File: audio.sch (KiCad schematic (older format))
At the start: 51 parts, among them J1601 SJ-43515TS, SW1301 MIC_CAM_HKS, U1601 SGTL5000, U1602 PAM8301, U1603 FSA6157L6X

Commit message: Update the schematic symbols and footprints after upgrading to KiCad 5.0.0, fix all ERC and DRC violations after the new update/upgrade
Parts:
- C1601, C1602, C1603, C1604, C1605, C1606, C1607, C1608, C1611, C1612, C1613, C1614, C1615, C1616, C1617, C1618, C1619, C1620, C1621, C1622, C1623, C1624, C1625: footprint Capacitors_SMD:C_0603 -> Capacitor_SMD:C_0603_1608Metric; symbol dvk-mx8m-bsb-rescue:C -> Device:C
- C1609, C1610: footprint Capacitors_Tantalum_SMD:CP_Tantalum_Case-S_EIA-3216-12_Reflow -> Capacitor_Tantalum_SMD:CP_EIA-3216-12_Kemet-S; symbol dvk-mx8m-bsb-rescue:CP1 -> Device:CP1
- D1601, D1602: symbol dvk-mx8m-bsb-rescue:D_TVS_ALT -> Device:D_TVS_ALT
- D1603: symbol dvk-mx8m-bsb-rescue:D_Zener_ALT -> Device:D_Zener_ALT
- FB1601, FB1602, FB1603: symbol dvk-mx8m-bsb-rescue:Ferrite_Bead -> Device:Ferrite_Bead
- FB1604, FB1605, FB1606, FB1607, FB1608: symbol dvk-mx8m-bsb-rescue:Ferrite_Bead_Small -> Device:Ferrite_Bead_Small
- LS1601: symbol dvk-mx8m-bsb-rescue:Speaker -> Device:Speaker
- MK1601: symbol dvk-mx8m-bsb-rescue:Microphone -> Device:Microphone
- R1601, R1602, R1603, R1604, R1605, R1606, R1607, R1608: footprint Resistors_SMD:R_0603 -> Resistor_SMD:R_0603_1608Metric; symbol dvk-mx8m-bsb-rescue:R -> Device:R
- SW1301: symbol dvk-mx8m-bsb-rescue:SW_DPDT_x2 -> Switch:SW_DPDT_x2
- U1602: symbol dvk-mx8m-bsb-rescue:PAM8301 -> Amplifier_Audio:PAM8301
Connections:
- wire segments 134 -> 171

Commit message: Replace the CMC-6022-37T microphoen with the CMC-2242PBL-A THT one since the old one cannot be surface mounted/reflowed, add the microphone's 3D model
The microphone's pin position/order is agrees with the manufacturer's "measurement circuit" from the datasheet such that the right (facing the top of the mic) terminal/pin is its GND (-).
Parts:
- MK1601: value CMC-6022 -> CMC-2242PBL; Distrib Link https://www.digikey.com/product-detail/en/cui-inc/CMC-6022-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 -> https://www.digikey.com/product-detail/en/cui-inc/CMC-2242P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; Distrib PN 102-4095-ND -> 102-1727-ND; MFG Part Num CMC-6022-37T -> CMC-2242PBL-A; Others https://www.digikey.com/products/en/audio-products/microphones/158?k=&pkeyword=&pv966=678&pv966=281&pv966=434&pv966=469&pv966=428&pv966=292&pv966=522&pv966=525&pv966=481&pv966=551&pv966=1658&pv966=330&pv966=415&pv966=1367&pv966=317&pv966=395&FV=a40062%2C9340003%2C1f140000%2Cyr100Hz+~+20kHz%7C2145%2Cyr100Hz+~+80kHz%7C2145%2Cyr20Hz+~+20kHz%7C2145%2Cyr25Hz+~+20kHz%7C2145%2Cyr28Hz+~+20kHz%7C2145%2Cyr35Hz+~+20kHz%7C2145%2Cyr50Hz+~+20kHz%7C2145%2Cyr60Hz+~+20kHz%7C2145%2Cyr6Hz+~+20kHz%7C2145%2Cyr70Hz+~+20kHz%7C2145%2Cyr75Hz+~+20kHz%7C2145%2Cffe0009e&quantity=0&ColumnSort=1000011&page=1&pageSize=500 -> https://www.digikey.com/products/en/audio-products/microphones/158?FV=fffc0066%2Cffe0009e&quantity=0&ColumnSort=1000011&page=1&pageSize=25
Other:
- note removed: "Add TVS next to int-mic?\n(OpenMoko does this)"
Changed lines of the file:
@@
 P 9000 5350
 F 0 "MK1601" H 8850 5400 50  0000 R CNN
-F 1 "CMC-6022" H 8850 5325 50  0000 R CNN
+F 1 "CMC-2242PBL" H 8850 5325 50  0000 R CNN
 F 2 "dvk-mx8m-bsb:Electret_Condenser_Mic_6mm" V 9000 5450 50  0001 C CNN
-F 3 "https://www.cui.com/product/resource/cmc-6022-37t.pdf" V 9000 5450 50  0001 C CNN
+F 3 "https://www.cui.com/product/resource/cmc-2242pbl-a.pdf" V 9000 5450 50  0001 C CNN
 F 4 "CUI" H 9000 5350 60  0001 C CNN "MFG Name"
-F 5 "CMC-6022-37T" H 9000 5350 60  0001 C CNN "MFG Part Num"
-F 6 "102-4095-ND" H 9000 5350 60  0001 C CNN "Distrib PN"
-F 7 "https://www.digikey.com/product-detail/en/cui-inc/CMC-6022-37T/102-4095-ND/6561033" H 9000 5350 60  0001 C CNN "Distrib Link"
+F 5 "CMC-2242PBL-A" H 9000 5350 60  0001 C CNN "MFG Part Num"
+F 6 "102-1727-ND" H 9000 5350 60  0001 C CNN "Distrib PN"
+F 7 "https://www.digikey.com/product-detail/en/cui-inc/CMC-2242PBL-A/102-1727-ND/1869987" H 9000 5350 60  0001 C CNN "Distrib Link"
 F 8 "±3dB" H 9000 5350 60  0001 C CNN "Tolerance"
-F 9 "https://www.digikey.com/products/en/audio-products/microphones/158?k=&pkeyword=&pv966=678&pv966=281&pv966=434&pv966=469&pv966=428&pv966=292&pv966=522&pv966=525&pv966=481&pv966=551&pv966=1658&pv966=330&pv966=415&pv966=1367&pv966=317&pv966=395&FV=a40062%2C9340003%2C1f140000%2Cyr100Hz+~+20kHz%7C2145%2Cyr100Hz+~+80kHz%7C2145%2Cyr20Hz+~+20kHz%7C2145%2Cyr25Hz+~+20kHz%7C2145%2Cyr28Hz+~+20kHz%7C2145%2Cyr35Hz+~+20kHz%7C2145%2Cyr50Hz+~+20kHz%7C2145%2Cyr60Hz+~+20kHz%7C2145%2Cyr6Hz+~+20kHz%7C2145%2Cyr70Hz+~+20kHz%7C2145%2Cyr75Hz+~+20kHz%7C2145%2Cffe0009e&quantity=0&ColumnSort=1000011&page=1&pageSize=500" H 9000 5350 60  0001 C CNN "Others"
+F 9 "https://www.digikey.com/products/en/audio-products/microphones/158?FV=fffc0066%2Cffe0009e&quantity=0&ColumnSort=1000011&page=1&pageSize=25" H 9000 5350 60  0001 C CNN "Others"
 	1    9000 5350
 	-1   0    0    -1
@@
 	6250 2400 6250 2150
 Connection ~ 6250 2150
-Text Notes 9100 5650 0    60   ~ 0
-Add TVS next to int-mic?\n(OpenMoko does this)
 Text Notes 6510 2290 0    60   ~ 0
 8Ω

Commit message: Add new built-in mic's frequency response curve to the schematic and re-simulate the HP_DET pin circuit with the protection diode's SPICE model included
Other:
- note added: "Simulation of HP_DET\nwithout HP jack inserted:"
- note removed: "Simulation of HP_DET @ 1kHz output\n without HP jack inserted:"

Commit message: Reduce all 0603 resistor sizes to 0402
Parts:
- R1601, R1602, R1603, R1604, R1605, R1606, R1607, R1608: footprint Resistor_SMD:R_0603_1608Metric -> Resistor_SMD:R_0402_1005Metric
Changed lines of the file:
@@
 F 0 "R1603" H 5025 3850 50  0000 C CNN
 F 1 "33" H 4975 3750 50  0000 C CNN
-F 2 "Resistor_SMD:R_0603_1608Metric" V 4780 3800 50  0001 C CNN
+F 2 "Resistor_SMD:R_0402_1005Metric" V 4780 3800 50  0001 C CNN
 F 3 "" H 4850 3800 50  0001 C CNN
 	1    4850 3800
@@
 F 0 "R1604" H 5725 3700 50  0000 C CNN
 F 1 "15k" H 5675 3600 50  0000 C CNN
-F 2 "Resistor_SMD:R_0603_1608Metric" V 5480 3650 50  0001 C CNN
+F 2 "Resistor_SMD:R_0402_1005Metric" V 5480 3650 50  0001 C CNN
 F 3 "" H 5550 3650 50  0001 C CNN
 	1    5550 3650
@@
 F 0 "R1605" H 6075 3850 50  0000 C CNN
 F 1 "33" H 6025 3750 50  0000 C CNN
-F 2 "Resistor_SMD:R_0603_1608Metric" V 5830 3800 50  0001 C CNN
+F 2 "Resistor_SMD:R_0402_1005Metric" V 5830 3800 50  0001 C CNN
 F 3 "" H 5900 3800 50  0001 C CNN
 	1    5900 3800
@@
 F 0 "R1606" H 6775 3700 50  0000 C CNN
 F 1 "15k" H 6725 3600 50  0000 C CNN
-F 2 "Resistor_SMD:R_0603_1608Metric" V 6530 3650 50  0001 C CNN
+F 2 "Resistor_SMD:R_0402_1005Metric" V 6530 3650 50  0001 C CNN
 F 3 "" H 6600 3650 50  0001 C CNN
 	1    6600 3650
@@
 F 0 "R1607" V 6500 5450 50  0000 C CNN
 F 1 "2.2k" V 6700 5450 50  0000 C CNN
-F 2 "Resistor_SMD:R_0603_1608Metric" V 6530 5450 50  0001 C CNN
+F 2 "Resistor_SMD:R_0402_1005Metric" V 6530 5450 50  0001 C CNN
 F 3 "" H 6600 5450 50  0001 C CNN
 	1    6600 5450
@@
 F 0 "R1608" H 9825 2900 50  0000 C CNN
 F 1 "1M" H 9750 2800 50  0000 C CNN
-F 2 "Resistor_SMD:R_0603_1608Metric" V 9580 2850 50  0001 C CNN
+F 2 "Resistor_SMD:R_0402_1005Metric" V 9580 2850 50  0001 C CNN
 F 3 "" H 9650 2850 50  0001 C CNN
 	1    9650 2850
@@
 F 0 "R1601" H 3625 3700 50  0000 C CNN
 F 1 "NC" H 3550 3600 50  0000 C CNN
-F 2 "Resistor_SMD:R_0603_1608Metric" V 3380 3650 50  0001 C CNN
+F 2 "Resistor_SMD:R_0402_1005Metric" V 3380 3650 50  0001 C CNN
 F 3 "" H 3450 3650 50  0001 C CNN
 	1    3450 3650
@@
 F 0 "R1602" H 4475 2600 50  0000 C CNN
 F 1 "100k" H 4450 2500 50  0000 C CNN
-F 2 "Resistor_SMD:R_0603_1608Metric" V 4230 2550 50  0001 C CNN
+F 2 "Resistor_SMD:R_0402_1005Metric" V 4230 2550 50  0001 C CNN
 F 3 "" H 4300 2550 50  0001 C CNN
 	1    4300 2550

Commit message: Change all 0603 capacitors _EXCEPT_ the 2.2uF, 4.7uF, 8.2uF, 10uF, and 22uF caps to 0402
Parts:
- C1602, C1603, C1604, C1605, C1606, C1608, C1612, C1613, C1614, C1615, C1616, C1617, C1618, C1619, C1620, C1621, C1622, C1623, C1624, C1625: footprint Capacitor_SMD:C_0603_1608Metric -> Capacitor_SMD:C_0402_1005Metric
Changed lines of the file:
@@
 F 0 "C1606" H 3925 3550 50  0000 L CNN
 F 1 "NC" H 3925 3350 50  0000 L CNN
-F 2 "Capacitor_SMD:C_0603_1608Metric" H 3938 3300 50  0001 C CNN
+F 2 "Capacitor_SMD:C_0402_1005Metric" H 3938 3300 50  0001 C CNN
 F 3 "" H 3900 3450 50  0001 C CNN
 	1    3900 3450
@@
 F 0 "C1608" H 4225 3550 50  0000 L CNN
 F 1 "NC" H 4225 3350 50  0000 L CNN
-F 2 "Capacitor_SMD:C_0603_1608Metric" H 4238 3300 50  0001 C CNN
+F 2 "Capacitor_SMD:C_0402_1005Metric" H 4238 3300 50  0001 C CNN
 F 3 "" H 4200 3450 50  0001 C CNN
 	1    4200 3450
@@
 F 0 "C1624" H 8425 3550 50  0000 L CNN
 F 1 "270pF" H 8425 3350 50  0000 L CNN
-F 2 "Capacitor_SMD:C_0603_1608Metric" H 8438 3300 50  0001 C CNN
+F 2 "Capacitor_SMD:C_0402_1005Metric" H 8438 3300 50  0001 C CNN
 F 3 "" H 8400 3450 50  0001 C CNN
 	1    8400 3450
@@
 F 0 "C1621" H 6925 3550 50  0000 L CNN
 F 1 "270pF" H 6925 3350 50  0000 L CNN
-F 2 "Capacitor_SMD:C_0603_1608Metric" H 6938 3300 50  0001 C CNN
+F 2 "Capacitor_SMD:C_0402_1005Metric" H 6938 3300 50  0001 C CNN
 F 3 "" H 6900 3450 50  0001 C CNN
 	1    6900 3450
@@
 F 0 "C1612" H 4875 3550 50  0000 L CNN
 F 1 "100nF" H 4875 3350 50  0000 L CNN
-F 2 "Capacitor_SMD:C_0603_1608Metric" H 4888 3300 50  0001 C CNN
+F 2 "Capacitor_SMD:C_0402_1005Metric" H 4888 3300 50  0001 C CNN
 F 3 "" H 4850 3450 50  0001 C CNN
 	1    4850 3450
@@
 F 0 "C1614" H 5225 3750 50  0000 L CNN
 F 1 "100pF" H 5225 3550 50  0000 L CNN
-F 2 "Capacitor_SMD:C_0603_1608Metric" H 5238 3500 50  0001 C CNN
+F 2 "Capacitor_SMD:C_0402_1005Metric" H 5238 3500 50  0001 C CNN
 F 3 "" H 5200 3650 50  0001 C CNN
 	1    5200 3650
@@
 F 0 "C1615" H 5925 3550 50  0000 L CNN
 F 1 "100nF" H 5925 3350 50  0000 L CNN
-F 2 "Capacitor_SMD:C_0603_1608Metric" H 5938 3300 50  0001 C CNN
+F 2 "Capacitor_SMD:C_0402_1005Metric" H 5938 3300 50  0001 C CNN
 F 3 "" H 5900 3450 50  0001 C CNN
 	1    5900 3450
@@
 F 0 "C1618" H 6275 3750 50  0000 L CNN
 F 1 "100pF" H 6275 3550 50  0000 L CNN
-F 2 "Capacitor_SMD:C_0603_1608Metric" H 6288 3500 50  0001 C CNN
+F 2 "Capacitor_SMD:C_0402_1005Metric" H 6288 3500 50  0001 C CNN
 F 3 "" H 6250 3650 50  0001 C CNN
 	1    6250 3650
@@
 F 0 "C1605" H 3125 3750 50  0000 L CNN
 F 1 "100nF" H 3125 3550 50  0000 L CNN
-F 2 "Capacitor_SMD:C_0603_1608Metric" H 3138 3500 50  0001 C CNN
+F 2 "Capacitor_SMD:C_0402_1005Metric" H 3138 3500 50  0001 C CNN
 F 3 "" H 3100 3650 50  0001 C CNN
 	1    3100 3650
@@
 F 0 "C1622" H 7325 5500 50  0000 L CNN
 F 1 "270pF" H 7325 5300 50  0000 L CNN
-F 2 "Capacitor_SMD:C_0603_1608Metric" H 7338 5250 50  0001 C CNN
+F 2 "Capacitor_SMD:C_0402_1005Metric" H 7338 5250 50  0001 C CNN
 F 3 "" H 7300 5400 50  0001 C CNN
 	1    7300 5400
@@
 F 0 "C1620" V 6725 5100 50  0000 L CNN
 F 1 "100nF" V 6550 5250 50  0000 L CNN
-F 2 "Capacitor_SMD:C_0603_1608Metric" H 6638 5050 50  0001 C CNN
+F 2 "Capacitor_SMD:C_0402_1005Metric" H 6638 5050 50  0001 C CNN
 F 3 "" H 6600 5200 50  0001 C CNN
 	1    6600 5200
@@
 F 0 "C1619" H 6425 5750 50  0000 L CNN
 F 1 "1uF" H 6425 5550 50  0000 L CNN
-F 2 "Capacitor_SMD:C_0603_1608Metric" H 6438 5500 50  0001 C CNN
+F 2 "Capacitor_SMD:C_0402_1005Metric" H 6438 5500 50  0001 C CNN
 F 3 "" H 6400 5650 50  0001 C CNN
 	1    6400 5650
@@
 F 0 "C1602" H 1875 1700 50  0000 L CNN
 F 1 "100nF" H 1875 1500 50  0000 L CNN
-F 2 "Capacitor_SMD:C_0603_1608Metric" H 1888 1450 50  0001 C CNN
+F 2 "Capacitor_SMD:C_0402_1005Metric" H 1888 1450 50  0001 C CNN
 F 3 "" H 1850 1600 50  0001 C CNN
 	1    1850 1600
@@
 F 0 "C1603" H 2525 1500 50  0000 L CNN
 F 1 "100nF" H 2525 1300 50  0000 L CNN
-F 2 "Capacitor_SMD:C_0603_1608Metric" H 2538 1250 50  0001 C CNN
+F 2 "Capacitor_SMD:C_0402_1005Metric" H 2538 1250 50  0001 C CNN
 F 3 "" H 2500 1400 50  0001 C CNN
 	1    2500 1400
@@
 F 0 "C1604" H 3125 2115 50  0000 L CNN
 F 1 "100nF" H 3125 1900 50  0000 L CNN
-F 2 "Capacitor_SMD:C_0603_1608Metric" H 3138 1850 50  0001 C CNN
+F 2 "Capacitor_SMD:C_0402_1005Metric" H 3138 1850 50  0001 C CNN
 F 3 "" H 3100 2000 50  0001 C CNN
 	1    3100 2000
@@
 F 0 "C1625" H 8625 4450 50  0000 L CNN
 F 1 "10nF" H 8625 4250 50  0000 L CNN
-F 2 "Capacitor_SMD:C_0603_1608Metric" H 8638 4200 50  0001 C CNN
+F 2 "Capacitor_SMD:C_0402_1005Metric" H 8638 4200 50  0001 C CNN
 F 3 "" H 8600 4350 50  0001 C CNN
 	1    8600 4350
@@
 F 0 "C1623" H 8225 4450 50  0000 L CNN
 F 1 "100nF" H 8225 4250 50  0000 L CNN
-F 2 "Capacitor_SMD:C_0603_1608Metric" H 8238 4200 50  0001 C CNN
+F 2 "Capacitor_SMD:C_0402_1005Metric" H 8238 4200 50  0001 C CNN
 F 3 "" H 8200 4350 50  0001 C CNN
 	1    8200 4350
@@
 F 0 "C1616" H 6075 2650 50  0000 L CNN
 F 1 "220pF" H 6075 2450 50  0000 L CNN
-F 2 "Capacitor_SMD:C_0603_1608Metric" H 6088 2400 50  0001 C CNN
+F 2 "Capacitor_SMD:C_0402_1005Metric" H 6088 2400 50  0001 C CNN
 F 3 "" H 6050 2550 50  0001 C CNN
 	1    6050 2550
@@
 F 0 "C1617" H 6275 2650 50  0000 L CNN
 F 1 "220pF" H 6275 2450 50  0000 L CNN
-F 2 "Capacitor_SMD:C_0603_1608Metric" H 6288 2400 50  0001 C CNN
+F 2 "Capacitor_SMD:C_0402_1005Metric" H 6288 2400 50  0001 C CNN
 F 3 "" H 6250 2550 50  0001 C CNN
 	1    6250 2550
@@
 F 0 "C1613" H 4925 1550 50  0000 L CNN
 F 1 "1uF" H 4925 1350 50  0000 L CNN
-F 2 "Capacitor_SMD:C_0603_1608Metric" H 4938 1300 50  0001 C CNN
+F 2 "Capacitor_SMD:C_0402_1005Metric" H 4938 1300 50  0001 C CNN
 F 3 "" H 4900 1450 50  0001 C CNN
 	1    4900 1450

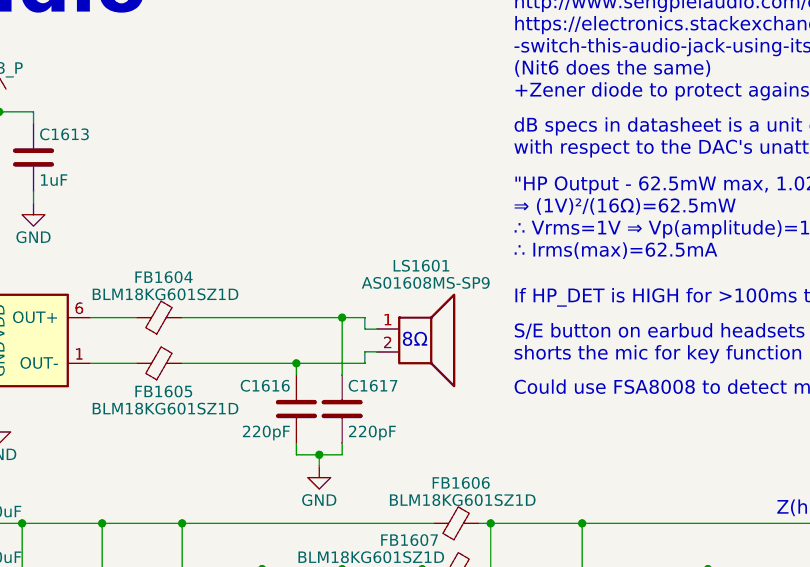
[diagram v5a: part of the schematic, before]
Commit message: Complete the HDMI circuit routing (including the pull-down NFETs and the diff pairs going to them)
The diff pairs going to the NFETs are exactly matched to 0 with their phase/skew; 1V8P still needs to be brought to them.
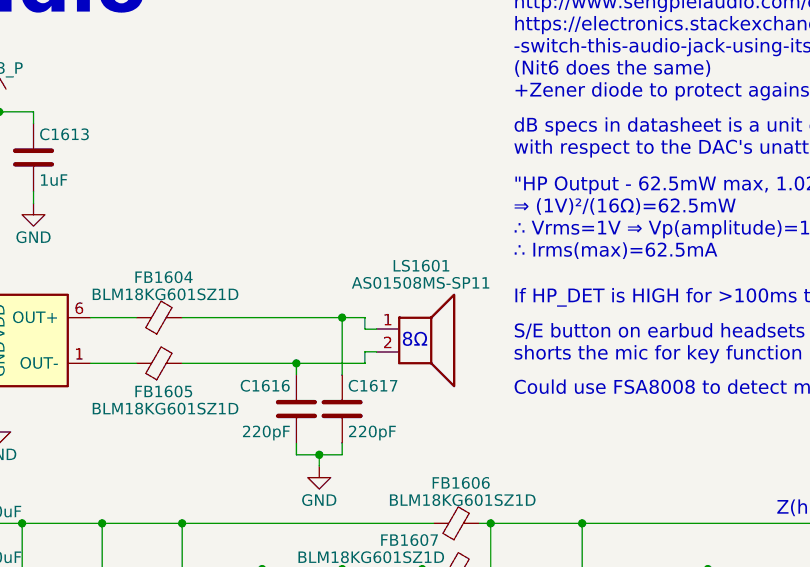
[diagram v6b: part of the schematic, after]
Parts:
- LS1601: value AS01608MS-SP9 -> AS01508MS-SP11
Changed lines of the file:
@@
 P 6600 2200
 F 0 "LS1601" H 6725 2475 50  0000 R CNN
-F 1 "AS01608MS-SP9" H 6900 2400 50  0000 R CNN
+F 1 "AS01508MS-SP11" H 6900 2400 50  0000 R CNN
 F 2 "dvk-mx8m-bsb:Speaker_flat_15x11x4mm" H 6600 2000 50  0001 C CNN
 F 3 "http://www.puiaudio.com/pdf/AS01508MS-SP11-WP-R.pdf" H 6590 2150 50  0001 C CNN
